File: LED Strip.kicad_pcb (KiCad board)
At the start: 2 copper layers, 21 x 12 mm, 9 parts, among them J1 CONN_01X02

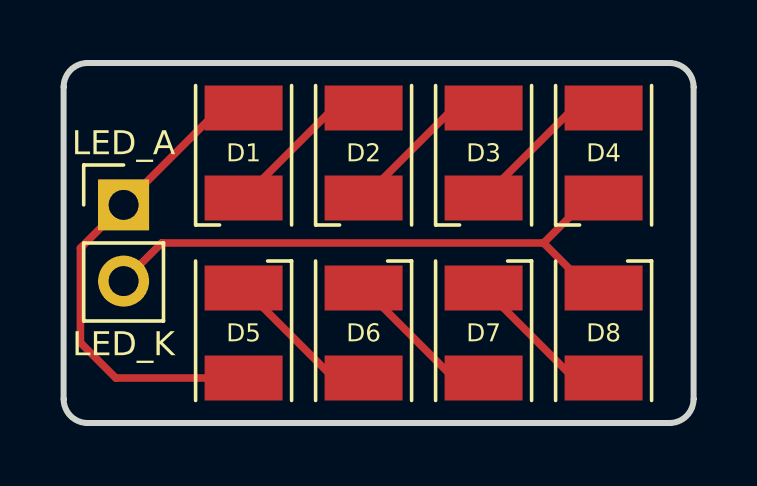
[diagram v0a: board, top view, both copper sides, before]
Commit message: Replaces LED_PLCC-2 packages with LED_0603
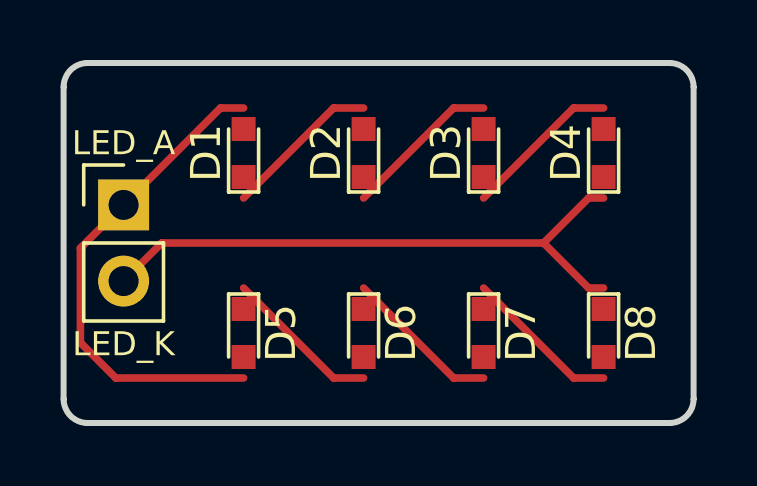
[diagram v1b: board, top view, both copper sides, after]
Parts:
- D1, D2, D3, D4, D5, D6, D7, D8: footprint LEDs:LED_PLCC-2 -> LEDs:LED_0603
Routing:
- net (no net): track 0.00 -> 31.5 mm
- net Net-(D7-Pad1): track 5.24 -> 0.00 mm
- net Net-(D6-Pad1): track 5.24 -> 0.00 mm
- net Net-(D5-Pad1): track 5.24 -> 0.00 mm
- net Net-(D3-Pad1): track 5.24 -> 0.00 mm
- net Net-(D2-Pad1): track 5.24 -> 0.00 mm
- net Net-(D1-Pad1): track 5.24 -> 0.00 mm

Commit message: Reduces overall footprint, cleans up placement of components and routes
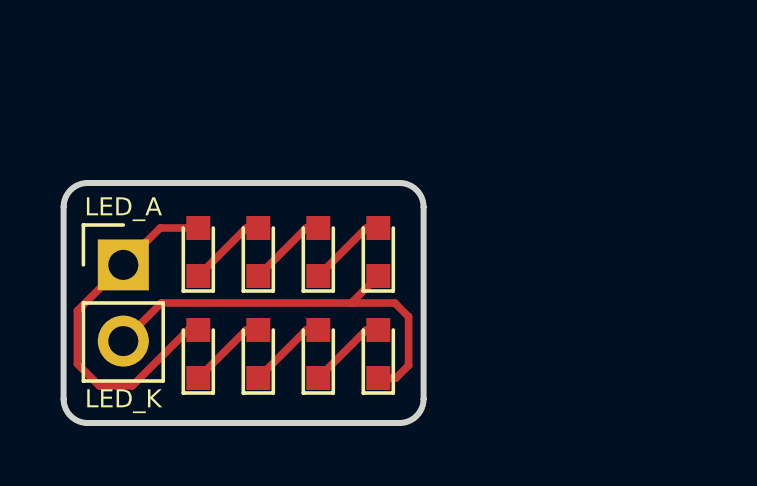
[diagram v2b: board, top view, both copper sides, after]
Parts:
- moved D4 8.20 mm to (110.5, 94.3)
- moved D8 7.54 mm to (110.5, 97.7), turned to 90 degrees
- moved D3 6.42 mm to (108.5, 94.3)
- moved D7 5.55 mm to (108.5, 97.7), turned to 90 degrees
- moved D2 4.82 mm to (106.5, 94.3)
- moved D1 3.63 mm to (104.5, 94.3)
- moved D6 3.58 mm to (106.5, 97.7), turned to 90 degrees
- moved J1 2.00 mm to (102.0, 94.7)
- moved D5 1.66 mm to (104.5, 97.7), turned to 90 degrees
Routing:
- net (no net): track 31.5 -> 0.00 mm
- net /LED_K: track 19.8 -> 14.4 mm
- net /LED_A: track 16.5 -> 12.0 mm
- net Net-(D7-Pad1): track 0.00 -> 2.66 mm
- net Net-(D6-Pad1): track 0.00 -> 2.66 mm
- net Net-(D5-Pad1): track 0.00 -> 2.66 mm
- net Net-(D3-Pad1): track 0.00 -> 2.66 mm
- net Net-(D2-Pad1): track 0.00 -> 2.66 mm
- net Net-(D1-Pad1): track 0.00 -> 2.66 mm
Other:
- board size 21 x 12 mm -> 12 x 8 mm

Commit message: Adds copper pours to top and bottom layers
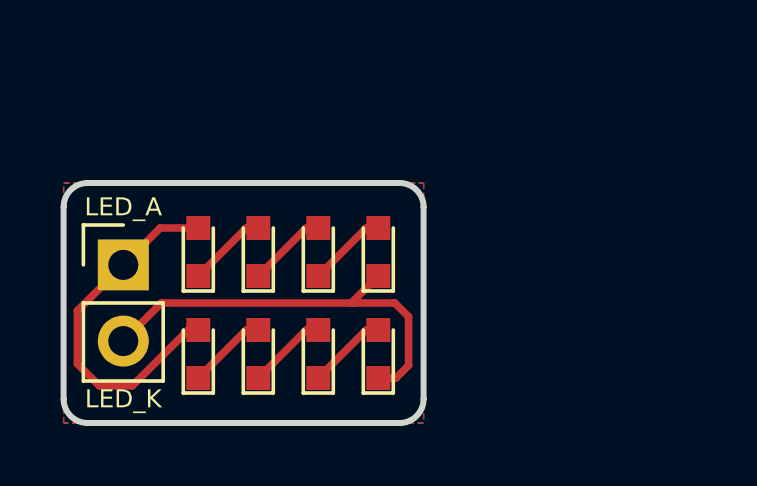
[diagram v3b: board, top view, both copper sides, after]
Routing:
- added copper zone on B.Cu, net (none)
- added copper zone on F.Cu, net (none)
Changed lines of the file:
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@@
     (links 10)
     (no_connects 0)
-    (area 99.899999 91.899999 112.100001 100.100001)
+    (area 96.902667 91.411 112.969 100.729)
     (thickness 1.6)
     (drawings 10)
@@
     (last_trace_width 0.254)
     (trace_clearance 0.254)
-    (zone_clearance 0.508)
+    (zone_clearance 0.254)
     (zone_45_only no)
     (trace_min 0.2)
@@
     (pad_to_mask_clearance 0.2)
     (aux_axis_origin 0 0)
+    (grid_origin 97.65 96.85)
     (visible_elements 7FFEFF7F)
     (pcbplotparams
@@
   (segment (start 104.49 95.1) (end 106.09 93.5) (width 0.254) (layer Top) (net 1))
   (segment (start 106.09 93.5) (end 106.49 93.5) (width 0.254) (layer Top) (net 1))
-  (segment (start 104.49 96.9) (end 104.15 96.9) (width 0.254) (layer Top) (net 2) (status C00000))
-  (segment (start 104.15 96.9) (end 102.29 98.76) (width 0.254) (layer Top) (net 2) (status 400000))
+  (segment (start 104.49 96.9) (end 104.15 96.9) (width 0.254) (layer Top) (net 2))
+  (segment (start 104.15 96.9) (end 102.29 98.76) (width 0.254) (layer Top) (net 2))
   (segment (start 102.29 98.76) (end 101.19 98.76) (width 0.254) (layer Top) (net 2))
   (segment (start 101.19 98.76) (end 100.46 98.03) (width 0.254) (layer Top) (net 2))
   (segment (start 100.46 98.03) (end 100.46 96.26) (width 0.254) (layer Top) (net 2))
-  (segment (start 100.46 96.26) (end 101.99 94.73) (width 0.254) (layer Top) (net 2) (status 800000))
-  (segment (start 101.99 94.73) (end 103.22 93.5) (width 0.254) (layer Top) (net 2) (status 400000))
-  (segment (start 103.22 93.5) (end 104.49 93.5) (width 0.254) (layer Top) (net 2) (status 800000))
+  (segment (start 100.46 96.26) (end 101.99 94.73) (width 0.254) (layer Top) (net 2))
+  (segment (start 101.99 94.73) (end 103.22 93.5) (width 0.254) (layer Top) (net 2))
+  (segment (start 103.22 93.5) (end 104.49 93.5) (width 0.254) (layer Top) (net 2))
   (segment (start 106.49 95.1) (end 108.09 93.5) (width 0.254) (layer Top) (net 3))
   (segment (start 108.09 93.5) (end 108.49 93.5) (width 0.254) (layer Top) (net 3))
@@
   (segment (start 106.49 98.5) (end 108.09 96.9) (width 0.254) (layer Top) (net 6))
   (segment (start 108.09 96.9) (end 108.49 96.9) (width 0.254) (layer Top) (net 6))
-  (segment (start 110.49 98.5) (end 111.08 98.5) (width 0.254) (layer Top) (net 7) (status 400000))
+  (segment (start 110.49 98.5) (end 111.08 98.5) (width 0.254) (layer Top) (net 7))
   (segment (start 111.04 96) (end 109.68 96) (width 0.254) (layer Top) (net 7))
   (segment (start 111.5 96.46) (end 111.04 96) (width 0.254) (layer Top) (net 7))
@@
   (segment (start 111.08 98.5) (end 111.5 98.08) (width 0.254) (layer Top) (net 7))
   (segment (start 109.68 96) (end 103.26 96) (width 0.254) (layer Top) (net 7))
-  (segment (start 103.26 96) (end 101.99 97.27) (width 0.254) (layer Top) (net 7) (status 800000))
+  (segment (start 103.26 96) (end 101.99 97.27) (width 0.254) (layer Top) (net 7))
   (segment (start 109.59 96) (end 109.68 96) (width 0.254) (layer Top) (net 7))
   (segment (start 109.59 96) (end 110.49 95.1) (width 0.254) (layer Top) (net 7))
   (segment (start 108.49 98.5) (end 110.09 96.9) (width 0.254) (layer Top) (net 8))
   (segment (start 110.09 96.9) (end 110.49 96.9) (width 0.254) (layer Top) (net 8))
+  (zone (net 0) (net_name "") (layer Top) (hatch edge 0.508)
+    (connect_pads (clearance 0.254))
+    (min_thickness 0.254)
+    (fill yes (arc_segments 16) (thermal_gap 0.508) (thermal_bridge_width 1.27) (smoothing fillet) (radius 0.127))
+    (polygon
+      (pts
+        (xy 112 100) (xy 100 100) (xy 100 92) (xy 112 92)
+      )
+    )
+  )
+  (zone (net 0) (net_name "") (layer Bottom) (hatch edge 0.508)
+    (connect_pads (clearance 0.254))
+    (min_thickness 0.254)
+    (fill yes (arc_segments 16) (thermal_gap 0.508) (thermal_bridge_width 1.27) (smoothing fillet) (radius 0.127))
+    (polygon
+      (pts
+        (xy 112 100) (xy 100 100) (xy 100 92) (xy 112 92)
+      )
+    )
+  )
 )

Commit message: Adds project name, version and OSH logo
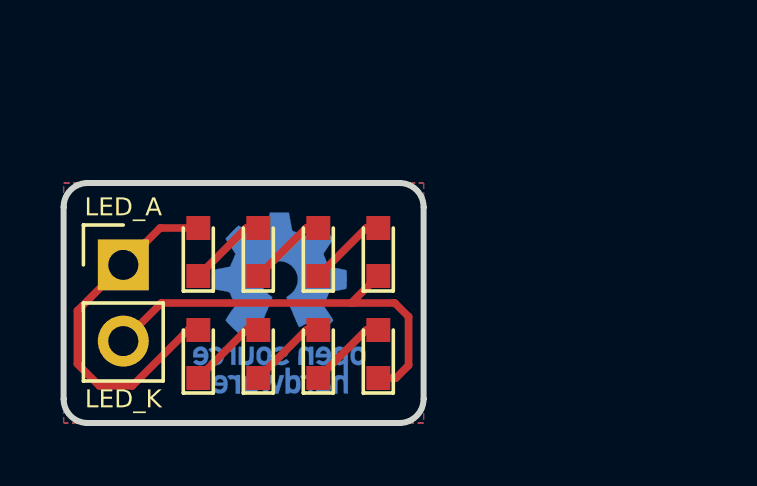
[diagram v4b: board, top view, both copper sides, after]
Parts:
- added OSHW-Logo: OSHW-Logo_5.7x6mm_Copper, Symbols:OSHW-Logo_5.7x6mm_Copper, B.Cu at (107.2, 96.0)
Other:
- board text added: "LED Strip QBLP601"
- board text added: "v1.0"
